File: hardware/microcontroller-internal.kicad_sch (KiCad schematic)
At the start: 19 parts, among them J5 1x2 jumper right-angle, J6 Conn_02x03_Odd_Even, J7 1x2 jumper right-angle, U15 74LVC138A, U17 74LVC138A

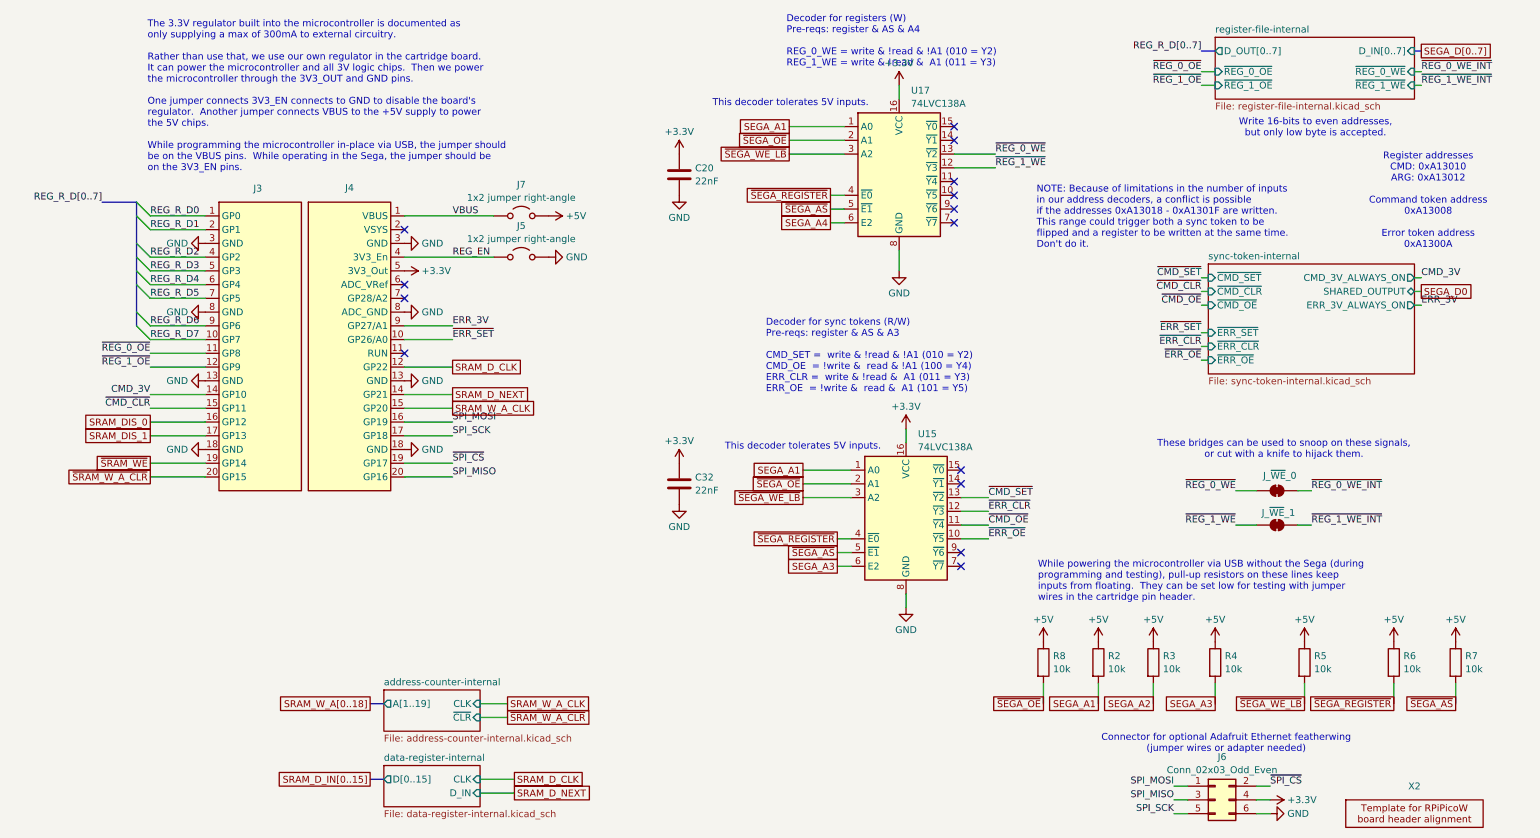
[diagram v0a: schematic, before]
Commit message: Reannotate schematics and drop debug bridges
Parts are now numbered starting at 0 for cart, 100 for SRAM, 300 for
microcontroller.

Also, drop debug bridges that made routing more difficult and had the
same names across prototype boards.

Hopefully this will help avoid naming conflicts for the unified PCB.

Also, redo prototype PCB layouts.

Now that all the names have changed, update board layouts.
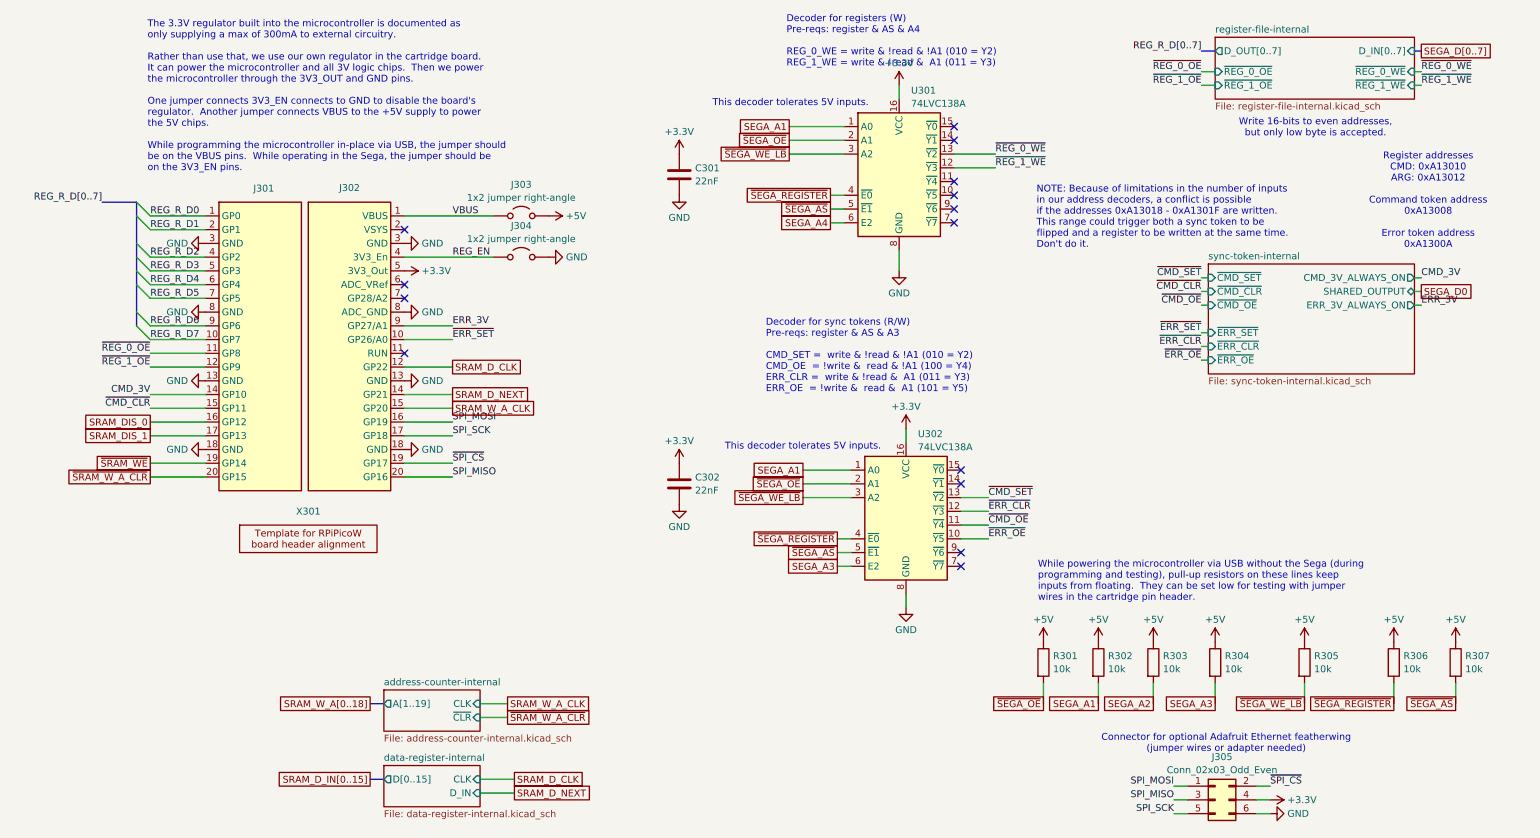
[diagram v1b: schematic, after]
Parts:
- removed J_~{WE}_0, J_~{WE}_1: ~, Jumper:SolderJumper-2_P1.3mm_Bridged_RoundedPad1.0x1.5mm, symbol Jumper:SolderJumper_2_Bridged
- renumbered C20 to C301, C32 to C302, J3 to J301, J4 to J302, J7 to J303, J5 to J304, J6 to J305, R8 to R301, R2 to R302, R3 to R303, R4 to R304, R5 to R305, R6 to R306, R7 to R307, U17 to U301, U15 to U302, X2 to X301
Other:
- note removed: "These bridges can be used to snoop on these signals, or cut with a knife to hijack them."
- moved on the sheet: X301
